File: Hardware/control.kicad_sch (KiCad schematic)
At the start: 5 parts, among them U1 RP2354B, X2 ABM8-272-T3

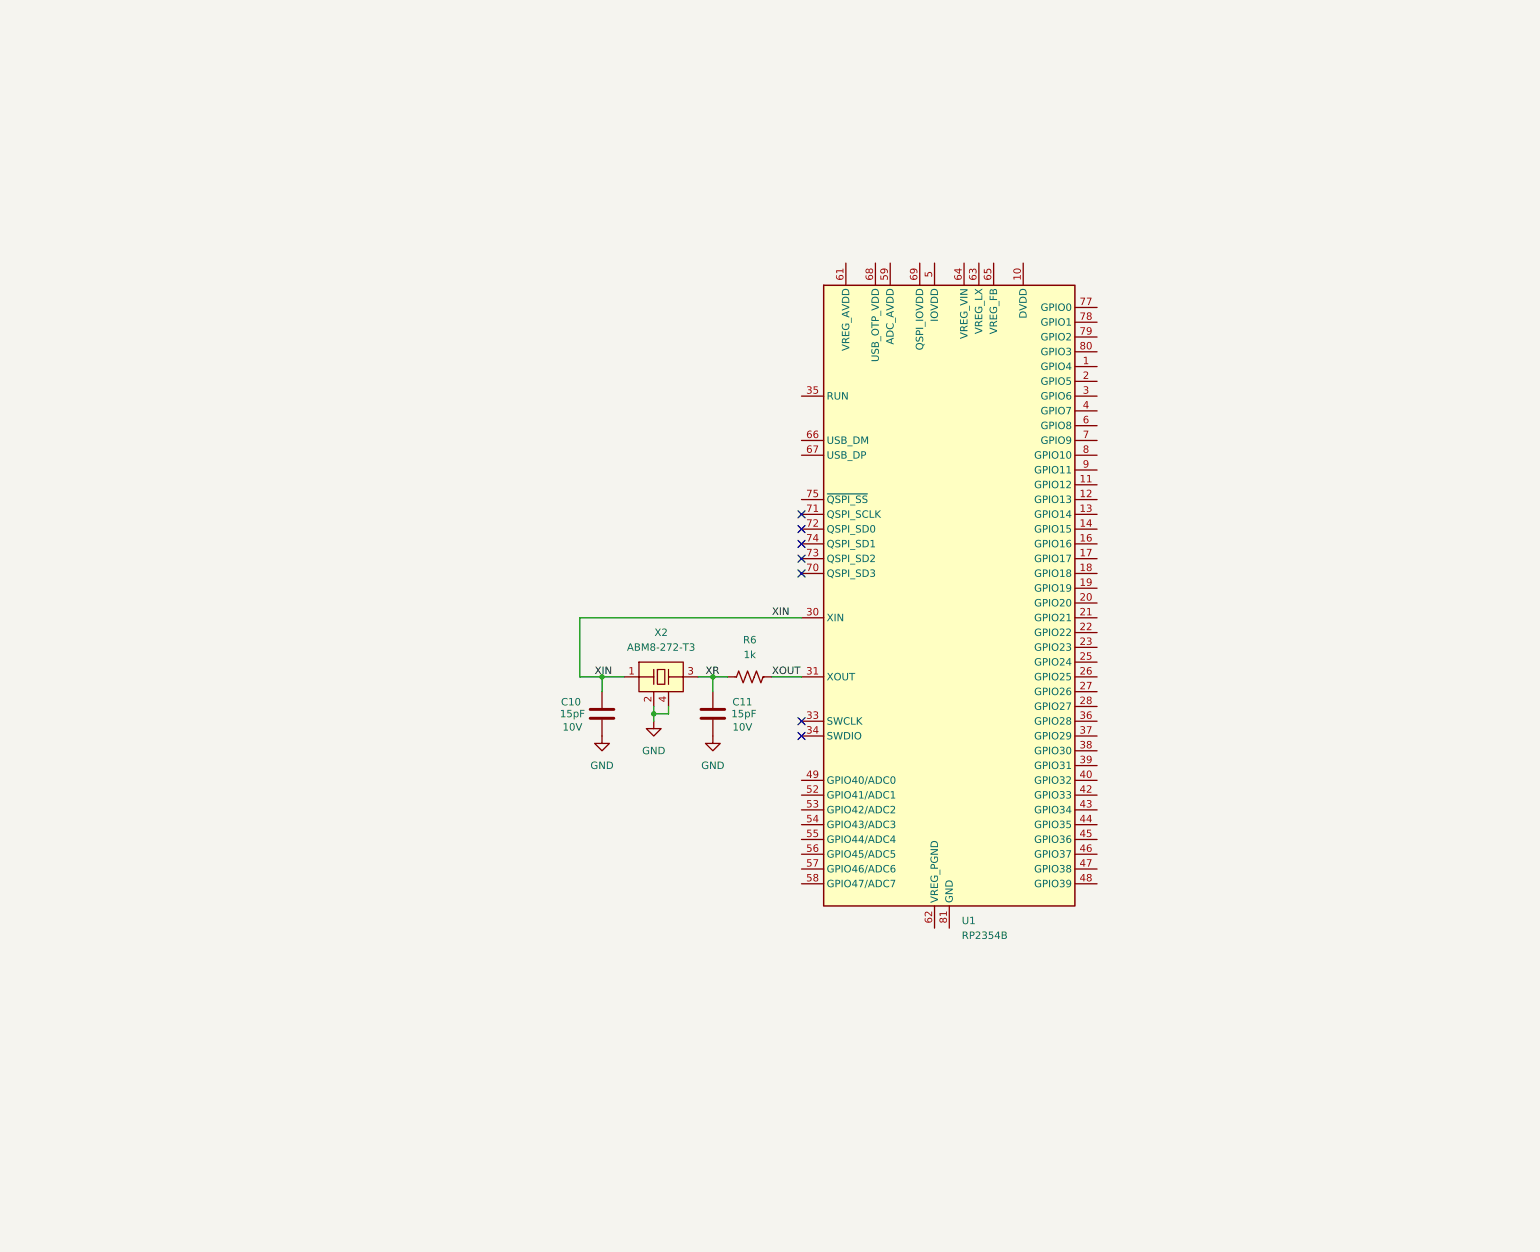
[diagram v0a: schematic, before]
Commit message: RP3254B power connections
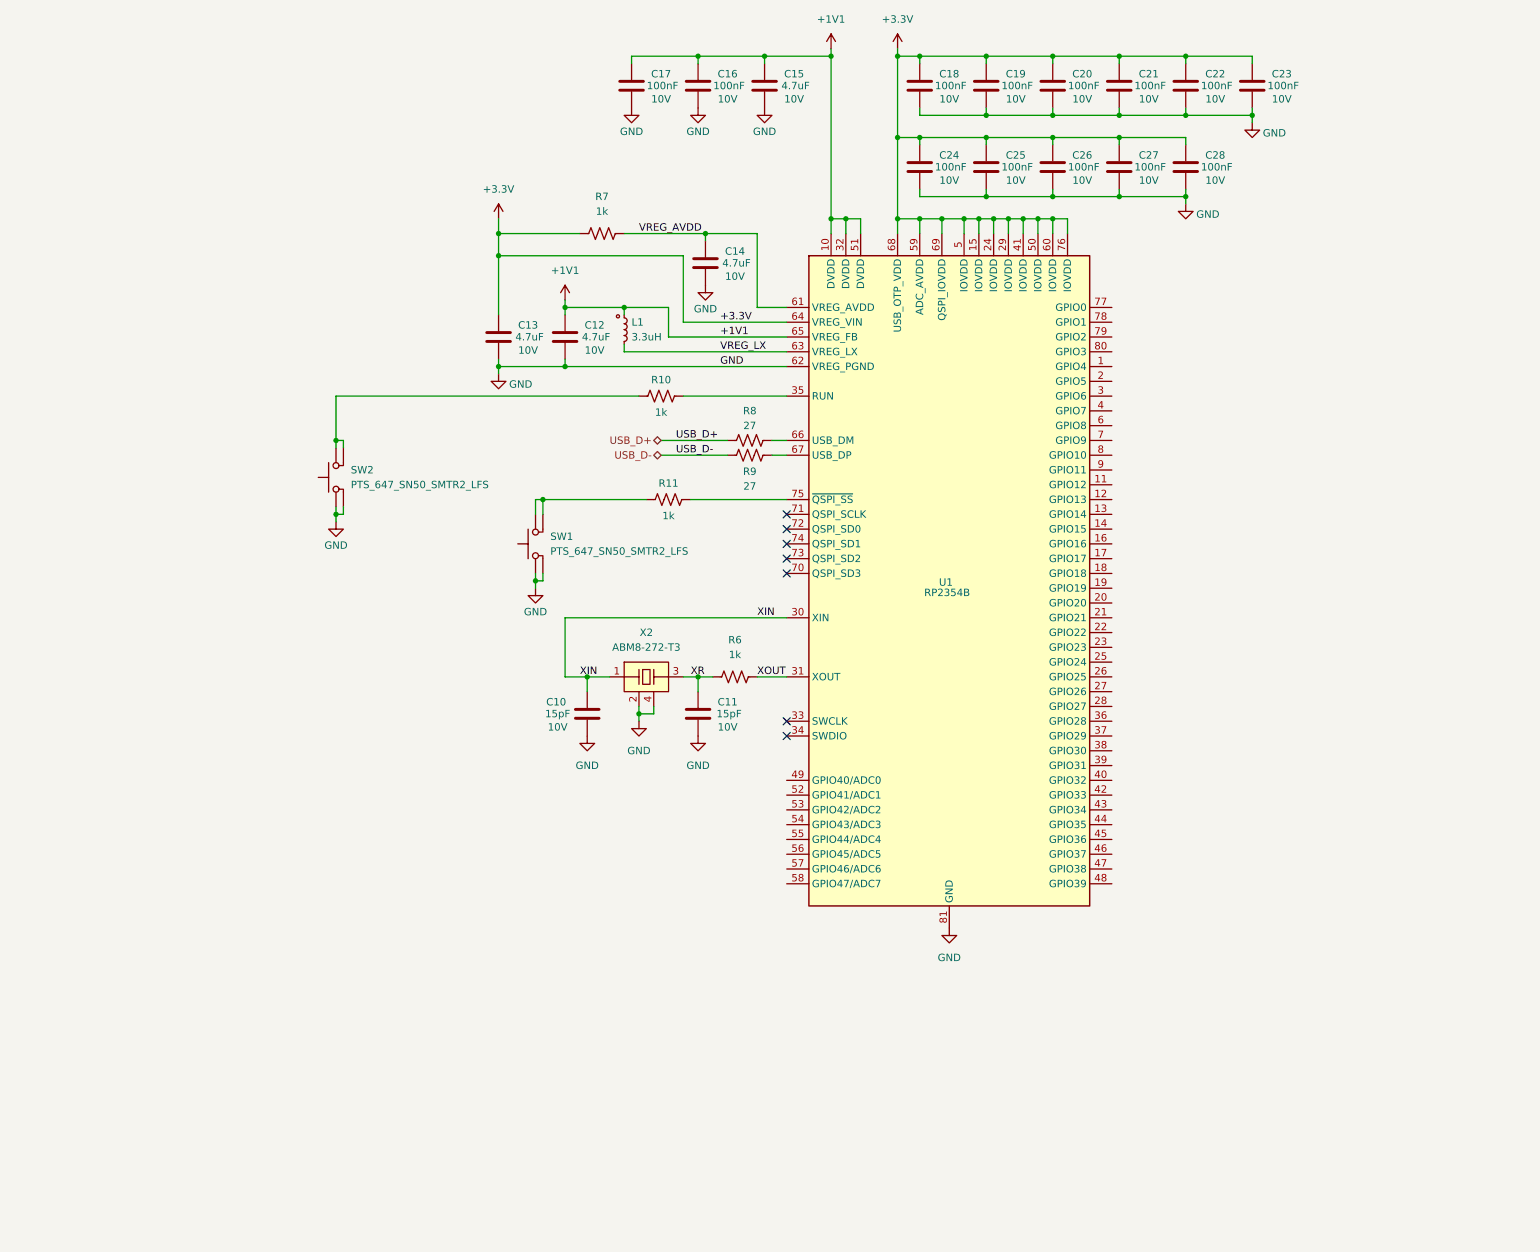
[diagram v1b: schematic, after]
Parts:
- added C12, C13, C14, C15: 4.7uF, symbol Device:C
- added C16, C17, C18, C19, C20, C21, C22, C23, C24, C25, C26, C27, C28: 100nF, symbol Device:C
- added L1: 3.3uH, symbol Device:L_Small
- added R10, R11, R7: 1k, symbol Device:R_US
- added R8, R9: 27, symbol Device:R_US
- added SW1, SW2: PTS_647_SN50_SMTR2_LFS, symbol Switch:SW_Push
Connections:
- net GND: now also U1.62 (VREG_PGND), U1.81 (GND), C12.2, C13.2, C14.2, C15.2, C16.2, C17.2, C18.2, C19.2, C20.2, C21.2, C22.2, C23.2, C24.2, C25.2, C26.2, C27.2, C28.2, SW1.1, SW1.2, SW2.1, SW2.2
- net +1V1: now reaches U1.10 (DVDD), U1.32 (DVDD), U1.51 (DVDD)
- net +1V1: now also U1.65 (VREG_FB), C12.1, C15.1, C16.1, C17.1, L1.1
- net +3.3V: now reaches U1.15 (IOVDD), U1.24 (IOVDD), U1.29 (IOVDD), U1.41 (IOVDD), U1.5 (IOVDD), U1.50 (IOVDD), U1.60 (IOVDD), U1.76 (IOVDD)
- net +3.3V: now also U1.59 (ADC_AVDD), U1.64 (VREG_VIN), U1.68 (USB_OTP_VDD), U1.69 (QSPI_IOVDD), C13.1, C18.1, C19.1, C20.1, C21.1, C22.1, C23.1, C24.1, C25.1, C26.1, C27.1, C28.1, R7.2
- net at U1.35 (RUN): now also R10.1
- net VREG_AVDD: now reaches U1.61 (VREG_AVDD)
- net VREG_AVDD: now also C14.1, R7.1
- net VREG_LX: now reaches U1.63 (VREG_LX)
- net VREG_LX: now also L1.2
- net at U1.66 (USB_DM): now also R8.1
- net at U1.67 (USB_DP): now also R9.1
- net at U1.75 (~{QSPI_SS}): now also R11.1
- new net: R10.2, SW2.3, SW2.4
- new net: R11.2, SW1.3, SW1.4
- new net USB_D+: R8.2
- new net USB_D-: R9.2
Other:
- moved on the sheet: C10, C11, R6, X2

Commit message: RP2354B interfaces
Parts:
- added C29: 100nF, symbol Device:C
- added J1: XKTF-015-N, symbol Connector:Micro_SD_Card_Det1
- added R12: 10k, symbol Device:R_US
- added SW3: PTS_647_SN50_SMTR2_LFS, symbol Switch:SW_Push
- R10, R11: value 1k -> 10k
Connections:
- net +3.3V: now also C29.1, J1.4 (VDD), SW3.3, SW3.4
- net GND: now also J1.6 (VSS), J1.SH (SHIELD), R12.2; no longer C17.2
- net SW1: now reaches U1.1 (GPIO4)
- net RDATA0: now reaches U1.11 (GPIO12)
- net RDATA1: now reaches U1.12 (GPIO13)
- net RDATA2: now reaches U1.13 (GPIO14)
- net RDATA3: now reaches U1.14 (GPIO15)
- net RDATA4: now reaches U1.16 (GPIO16)
- net RDATA5: now reaches U1.17 (GPIO17)
- net RDATA6: now reaches U1.18 (GPIO18)
- net RDATA7: now reaches U1.19 (GPIO19)
- net SW2: now reaches U1.2 (GPIO5)
- net ~{ROMEN}: now reaches U1.20 (GPIO20)
- net INTR: now reaches U1.21 (GPIO21)
- net ROM_ADDR0: now reaches U1.22 (GPIO22)
- net ROM_ADDR1: now reaches U1.23 (GPIO23)
- net ROM_ADDR2: now reaches U1.25 (GPIO24)
- net ROM_ADDR3: now reaches U1.26 (GPIO25)
- net ROM_ADDR4: now reaches U1.27 (GPIO26)
- net ROM_ADDR5: now reaches U1.28 (GPIO27)
- net SW3: now reaches U1.3 (GPIO6)
- net ROM_ADDR6: now reaches U1.36 (GPIO28)
- net ROM_ADDR7: now reaches U1.37 (GPIO29)
- net ROM_ADDR8: now reaches U1.38 (GPIO30)
- net ROM_ADDR9: now reaches U1.39 (GPIO31)
- net SW4: now reaches U1.4 (GPIO7)
- net ROM_ADDR10: now reaches U1.40 (GPIO32)
- net ROM_ADDR11: now reaches U1.42 (GPIO33)
- net ROM_ADDR12: now reaches U1.43 (GPIO34)
- net ROM_ADDR13: now reaches U1.44 (GPIO35)
- net SDATA: now reaches U1.45 (GPIO36)
- net FSYNC: now reaches U1.46 (GPIO37)
- net BCLK: now reaches U1.47 (GPIO38)
- net at U1.48 (GPIO39): now also C29.2, R12.1, SW3.1, SW3.2
- net SD_MISO: now reaches U1.49 (GPIO40/ADC0)
- net SD_MISO: now also J1.7 (DAT0)
- net ~{SD_CS}: now reaches U1.52 (GPIO41/ADC1)
- net ~{SD_CS}: now also J1.2 (DAT3/CD)
- net SD_SCK: now reaches U1.53 (GPIO42/ADC2)
- net SD_SCK: now also J1.5 (CLK)
- net SD_MOSI: now reaches U1.54 (GPIO43/ADC3)
- net SD_MOSI: now also J1.3 (CMD)
- net SW5: now reaches U1.6 (GPIO8)
- net SW6: now reaches U1.7 (GPIO9)
- net DIGITALKER_CLK_4MHZ: now reaches U1.77 (GPIO0)
- net ~{DIGITALKER_CS}: now reaches U1.78 (GPIO1)
- net ~{DIGITALKER_WR}: now reaches U1.79 (GPIO2)
- net SW7: now reaches U1.8 (GPIO10)
- net DIGITALKER_CMS: now reaches U1.80 (GPIO3)
- net SW8: now reaches U1.9 (GPIO11)
- new net SD_DET: J1.9 (DET)
- no-connect marks 7 -> 9
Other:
- note added: "BOOTSEL"
- note added: "RESET"
- moved on the sheet: C10, C11, C12, C13, C14, C15, C16, C17, C18, C19, C20, C21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

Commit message: sync
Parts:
- added C30: 100nF, symbol Device:C
- added D1: 150060VS75000, symbol LED:CQY99
- added R13: 132, symbol Device:R_US
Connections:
- net +3.3V: now also C30.1
- net GND: now also C30.2, D1.1 (K)
- net BUTTON: now reaches C29.2, R12.1, SW3.1, SW3.2, U1.48 (GPIO39)
- net LED: now reaches U1.58 (GPIO47/ADC7)
- net LED: now also R13.1
- new net: D1.2 (A), R13.2

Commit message: sync
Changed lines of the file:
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@@
 	)
 	(hierarchical_label "INTR"
-		(shape output)
+		(shape input)
 		(at 259.08 138.43 0)
 		(effects
@@
 	)
 	(hierarchical_label "~{ROMEN}"
-		(shape output)
+		(shape input)
 		(at 259.08 135.89 0)
 		(effects
@@
 	)
 	(hierarchical_label "ROM_ADDR[0..13]"
-		(shape output)
+		(shape input)
 		(at 271.78 135.89 0)
 		(effects
